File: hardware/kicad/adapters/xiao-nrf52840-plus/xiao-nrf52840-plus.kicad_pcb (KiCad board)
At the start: 2 copper layers, 76 x 38 mm, 7 parts, among them J1 COMMON_MCU_ADAPTER_2x10

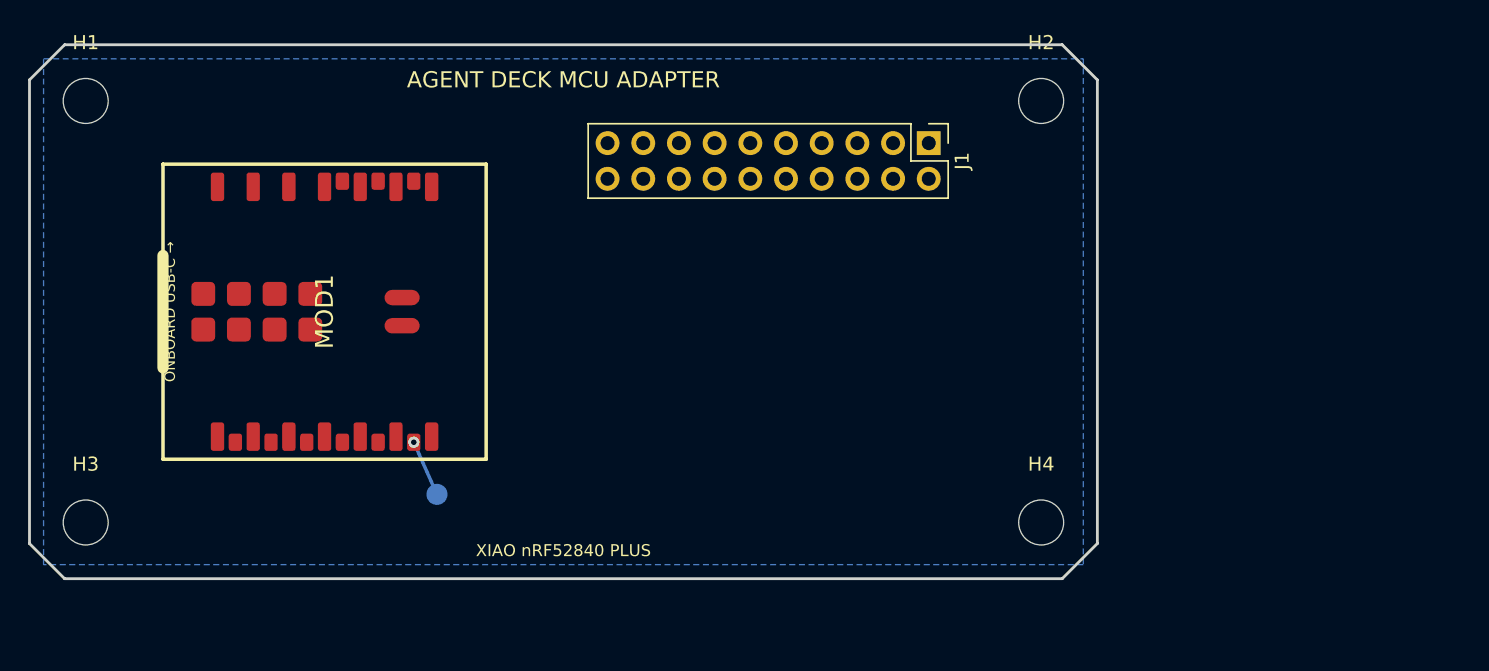
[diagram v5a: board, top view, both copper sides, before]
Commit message: Establish a host-verified V1 baseline before physical bring-up
Constraint: The common PCB remains 100 mm square, all controls stay PCB-mounted, and no display is added.
Rejected: Deterministic adapter autorouting | KiCad exposed real escape and via conflicts, so reviewed manual routing remains explicit.
Confidence: medium
Scope-risk: broad
Directive: Do not order boards until all open connections are routed, complete schematics pass parity, exact parts pass sample fit, and physical power/RF/USB/BLE tests succeed.
Tested: KiCad block ERC 0 on three projects; DRC 0 errors with documented warnings and open nets; Blender manifold STL generation; firmware 12/12 normal, sanitized, and embedded-style builds; bridge 41/41 on Python 3.11 and 3.14.
Not-tested: Physical XIAO USB/BLE, RF, battery charging and swelling, touch sensitivity, connector mating, real audio backend, and assembled endurance.
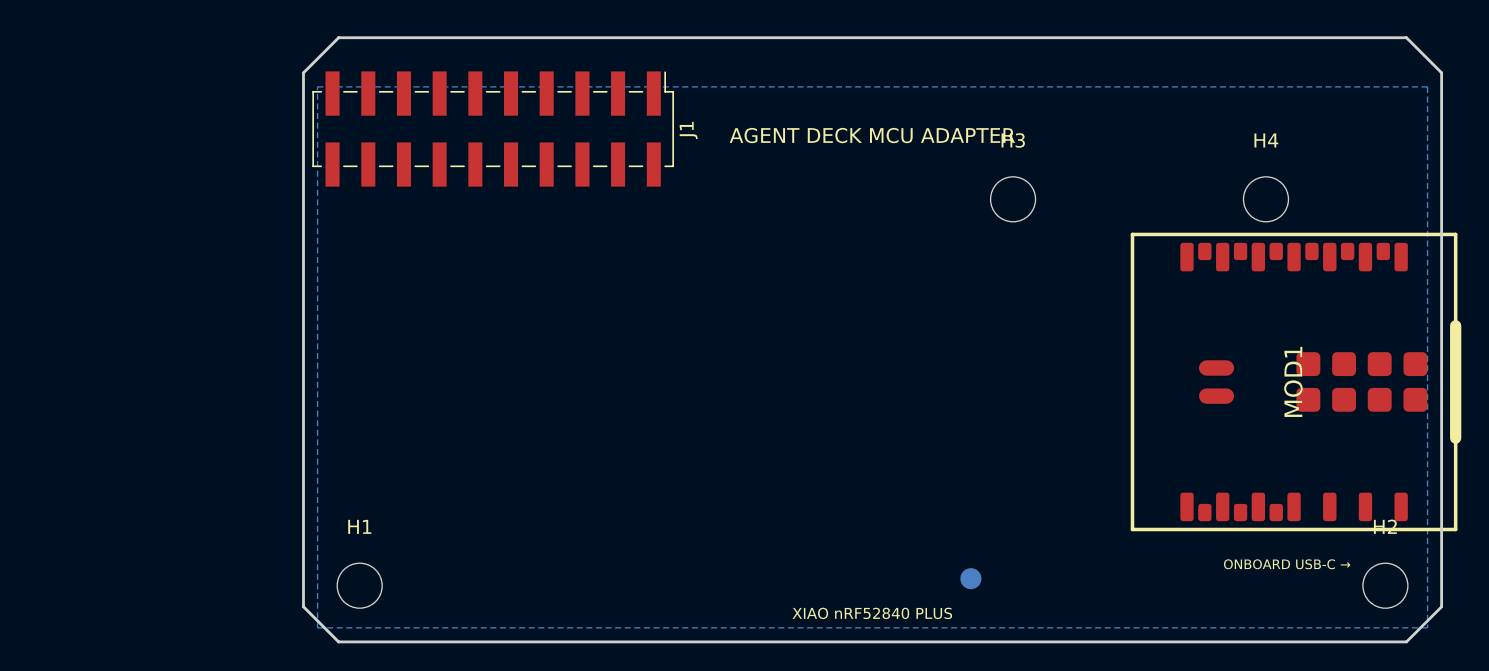
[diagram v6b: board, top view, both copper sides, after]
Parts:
- J1: value COMMON_MCU_ADAPTER_2x10 -> COMMON_MCU_ADAPTER_2x10 / Samtec TSM-110-04-L-DV fit-check candidate; footprint PinHeader_2x10_P2.54mm_Vertical -> PinHeader_2x10_P2.54mm_Vertical_SMD
- moved H3 69.9 mm to (80.0, 21.0)
- moved MOD1 69.2 mm to (100.0, 34.0), turned to -90 degrees
- moved H2 42.3 mm to (106.5, 48.5)
- moved H1 39.6 mm to (33.5, 48.5)
- moved TP1 38.5 mm to (77.0, 48.0)
- moved J1 31.0 mm to (43.0, 16.0)
- moved H4 28.0 mm to (98.0, 21.0)
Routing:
- net BAT_SENSE_D16_RESERVED: track 4.06 -> 0.00 mm, vias 1 -> 0
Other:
- board size 76 x 38 mm -> 81 x 43 mm
- board text added: "FIT-CHECK / ROUTING DRAFT"
- board text added: "XIAO RF KEEP-OUT"
- board text removed: "PLACEMENT / NETLIST DRAFT"
